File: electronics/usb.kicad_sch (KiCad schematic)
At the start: 16 parts, among them J1 TYPE-C-31-M-12, U1 USBLC6-2SC6, U2 AP22818AKEWT

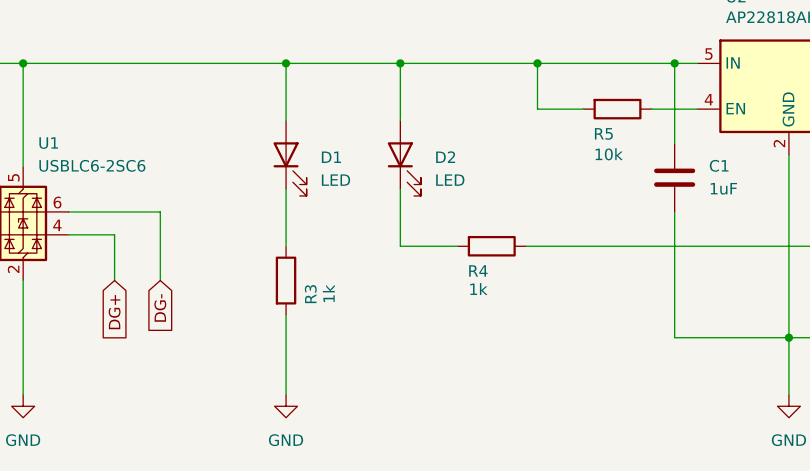
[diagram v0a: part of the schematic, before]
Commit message: Added IO3 pullup and negative 3V3 rail testpoint, few other PCB laypu… (#4)
* Added IO3 pullup and negative 3V3 rail testpoint, few other PCB layput improvements.
* Updated exports - gerbers, schematics, bom, CPL KiCad for version 1.3.1

---------

Signed-off-by: Maxim Pavlov <max.eelabs@gmail.com>
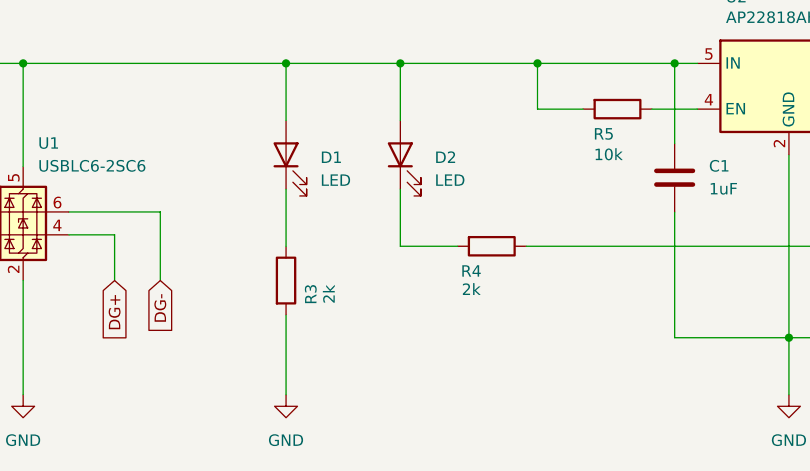
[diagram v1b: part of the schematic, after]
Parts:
- R3, R4: value 1k -> 2k
- TP1, TP2, TP3: now left out of the parts list
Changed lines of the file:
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@@
 		(title "PSU-EXT USB")
 		(date "2026-08-08")
-		(rev "1.3.0")
+		(rev "1.3.1")
 		(company "MaxEELabs")
 		(comment 3 "This hardware design is licensed under CERN-OHL-S v2.\nCopyright © 2026 PSU-EXT Authors: https://github.com/PSU-Ext-Org")
@@
 		(dnp no)
 		(property "Reference" "R4"
-			(at 155.956 57.404 90)
-			(show_name no)
-			(do_not_autoplace no)
-			(effects
-				(font
-					(size 1.27 1.27)
-				)
-			)
-		)
-		(property "Value" "1k"
-			(at 155.956 59.436 90)
+			(at 155.194 57.404 90)
+			(show_name no)
+			(do_not_autoplace no)
+			(effects
+				(font
+					(size 1.27 1.27)
+				)
+			)
+		)
+		(property "Value" "2k"
+			(at 155.194 59.436 90)
 			(show_name no)
 			(do_not_autoplace no)
@@
 			)
 		)
-		(property "Value" "1k"
+		(property "Value" "2k"
 			(at 139.446 59.944 90)
 			(show_name no)
@@
 		(body_style 1)
 		(exclude_from_sim no)
-		(in_bom yes)
+		(in_bom no)
 		(on_board yes)
-		(in_pos_files yes)
+		(in_pos_files no)
 		(dnp no)
 		(property "Reference" "TP1"
@@
 		(body_style 1)
 		(exclude_from_sim no)
-		(in_bom yes)
+		(in_bom no)
 		(on_board yes)
-		(in_pos_files yes)
+		(in_pos_files no)
 		(dnp no)
 		(fields_autoplaced yes)
@@
 		(body_style 1)
 		(exclude_from_sim no)
-		(in_bom yes)
+		(in_bom no)
 		(on_board yes)
-		(in_pos_files yes)
+		(in_pos_files no)
 		(dnp no)
 		(fields_autoplaced yes)
